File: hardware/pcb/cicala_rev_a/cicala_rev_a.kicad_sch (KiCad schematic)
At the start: 0 parts

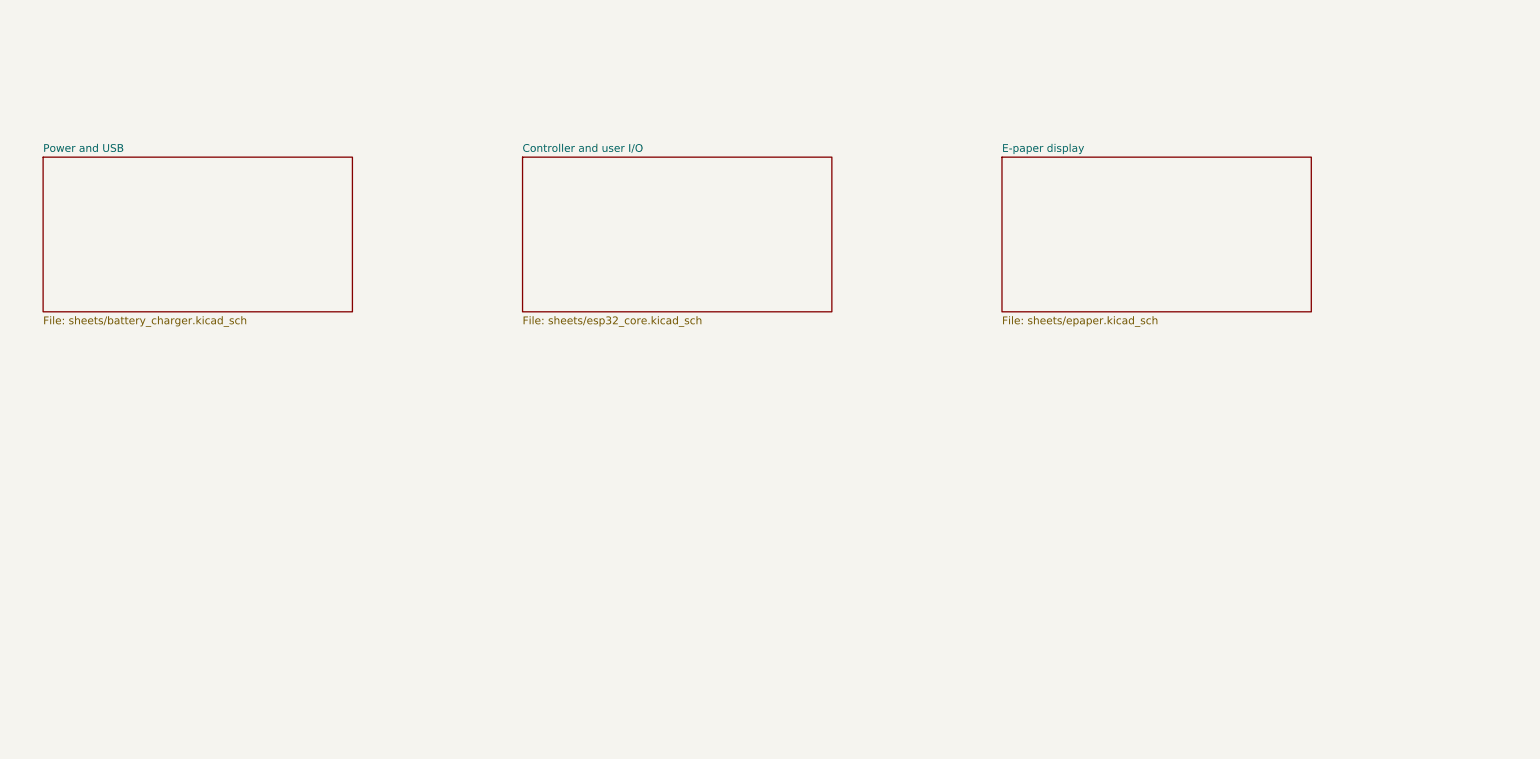
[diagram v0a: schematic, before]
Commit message: refactor(hw): make the root sheet a real hierarchy
The root was three boxes and a filename; every cross-sheet signal travelled
by global label, so nothing recorded which block produced a signal and which
consumed it. The 19 nets that actually cross a sheet boundary are now
hierarchical: each child carries a directional hierarchical label and the
root carries the matching sheet pin, wired block to block. The root also
states the power flow in words.

GND stays global; a ground symbol reads better than a pin on every block.
Root-level global labels keep the plain net names that pin_contract.csv and
the firmware refer to, rather than the sheet-path names a local label gives.

Connectivity is unchanged: the exported netlist is identical to the one
before the conversion, net for net and pin for pin.

Also hides the PWR_FLAG references, moves the USB shield network and the
cell-current link inside the blocks they belong to, and gives every page the
same company, revision and date.

Co-Authored-By: Claude Opus 5 <noreply@anthropic.com>
Claude-Session: https://claude.ai/code/session_01E5vy1HJsPztSk9nFw6j5Ko
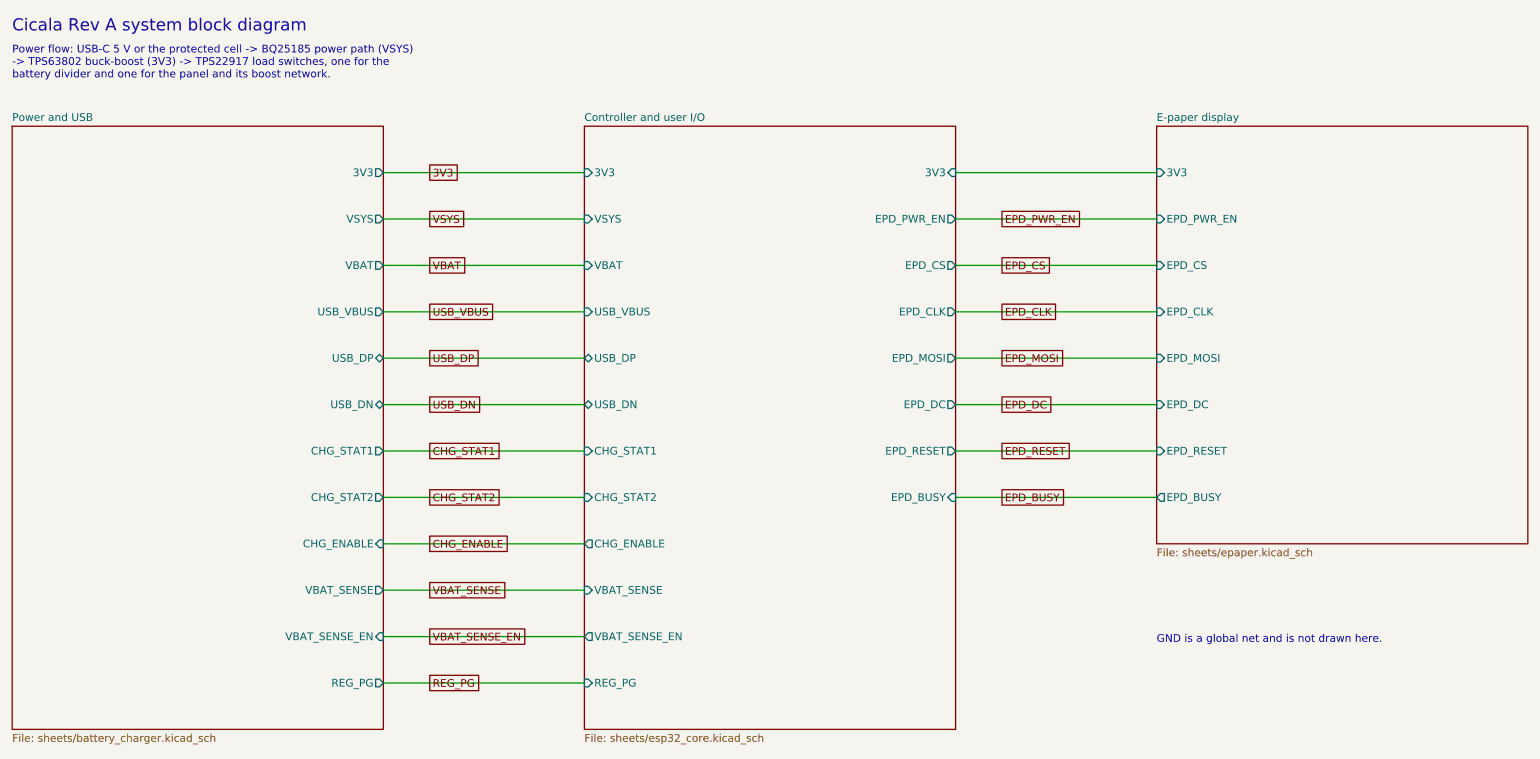
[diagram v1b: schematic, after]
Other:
- sheet Controller and user I/O ports: added 3V3, CHG_ENABLE, CHG_STAT1, CHG_STAT2, EPD_BUSY, EPD_CLK, EPD_CS, EPD_DC, EPD_MOSI, EPD_PWR_EN, EPD_RESET, REG_PG, USB_DN, USB_DP, USB_VBUS, VBAT, VBAT_SENSE, VBAT_SENSE_EN, VSYS; removed none
- sheet E-paper display ports: added 3V3, EPD_BUSY, EPD_CLK, EPD_CS, EPD_DC, EPD_MOSI, EPD_PWR_EN, EPD_RESET; removed none
- sheet Power and USB ports: added 3V3, CHG_ENABLE, CHG_STAT1, CHG_STAT2, REG_PG, USB_DN, USB_DP, USB_VBUS, VBAT, VBAT_SENSE, VBAT_SENSE_EN, VSYS; removed none
- note added: "Cicala Rev A system block diagram"
- note added: "GND is a global net and is not drawn here."
- note added: "Power flow: USB-C 5 V or the protected cell -> BQ25185 power path (VSYS) -> TPS63802 buck-boost (3V3) -> TPS22917 load switches, one for the battery divider and one for the panel and its boost network."
- company: (none) -> Cicala
